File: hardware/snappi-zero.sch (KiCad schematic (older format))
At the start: 0 parts

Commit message: Design schematic.
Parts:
- added P1: CONN_02X40, symbol CONN_02X40
- added R1: 10k, symbol R
- added U1: RF200, symbol RF200
- added U2: SM220UF1, symbol SM220UF1
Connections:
- new net 3v3: P1.1 (P1), R1.1, U1.21 (VCC), U2.A2 (VCC), U2.A3 (VCC)
- new net GND: P1.9 (P9), U1.1 (GND), U1.24 (GND), U2.A1 (GND), U2.A8 (GND), U2.B8 (GND), U2.D8 (GND), U2.F8 (GND), U2.G8 (GND), U2.H1 (GND), U2.H8 (GND)
- new net GPIO_17: P1.11 (P11), R1.2, U1.23 (~RESET), U2.H5 (RESET)
- new net LED_A: U1.2 (GPIO0), U2.D1 (GPIO_5)
- new net LED_B: U1.3 (GPIO1), U2.D2 (GPIO_6)
- new net LED_C: U1.4 (GPIO2), U2.D3 (GPIO_7)
- new net PI_RX: P1.12 (P12), U1.10 (GPIO8)
- new net PI_TX: P1.10 (P10), U1.9 (GPIO7)
- no-connect marks 0 -> 120

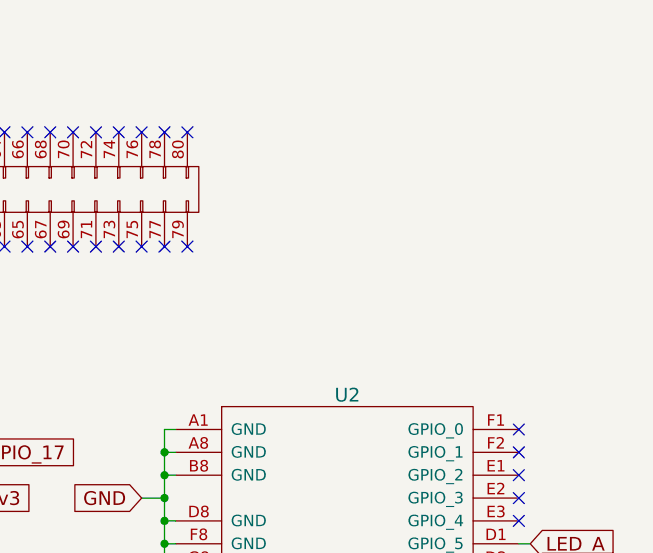
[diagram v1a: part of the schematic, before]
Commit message: Add LEDs and footprint assignment.
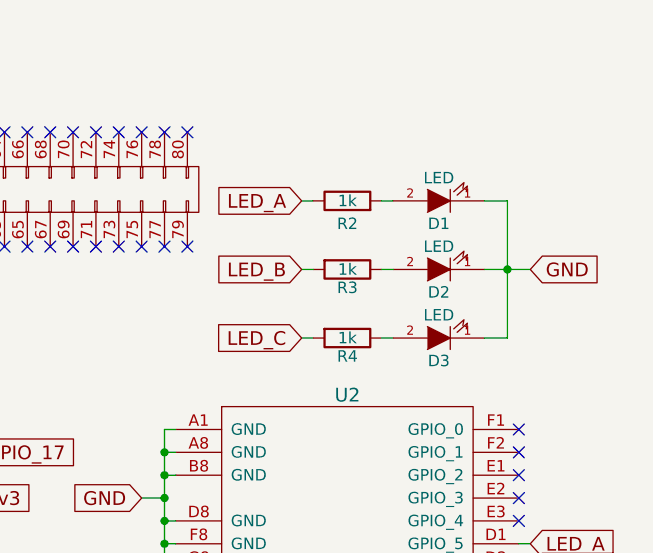
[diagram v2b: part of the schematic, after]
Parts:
- added D1, D2, D3: LED, LEDs:LED_1206, symbol LED
- added R2, R3, R4: 1k, Resistors_SMD:R_0805_HandSoldering, symbol R
- P1: footprint (none) -> Socket_Strips:Socket_Strip_Straight_2x40
- R1: footprint (none) -> Resistors_SMD:R_0805_HandSoldering
- U1: footprint (none) -> CrumpPrints:RF200
- U2: footprint (none) -> CrumpPrints:SM200
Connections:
- net GND: now also D1.1 (K), D2.1 (K), D3.1 (K)
- net LED_A: now also R2.1
- net LED_B: now also R3.2
- net LED_C: now also R4.2
- new net: D1.2 (A), R2.2
- new net: D2.2 (A), R3.1
- new net: D3.2 (A), R4.1
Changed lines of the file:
@@
 F 0 "P1" H 5400 3850 50  0000 C CNN
 F 1 "CONN_02X40" V 5400 1800 50  0000 C CNN
-F 2 "" H 5400 1800 50  0000 C CNN
+F 2 "Socket_Strips:Socket_Strip_Straight_2x40" H 5400 1800 50  0001 C CNN
 F 3 "" H 5400 1800 50  0000 C CNN
 	1    5400 1800
@@
 F 0 "U1" H 5500 2650 60  0000 C CNN
 F 1 "RF200" H 5500 4150 60  0000 C CNN
-F 2 "" H 5450 3400 60  0000 C CNN
+F 2 "CrumpPrints:RF200" H 5450 3400 60  0001 C CNN
 F 3 "" H 5450 3400 60  0000 C CNN
 	1    5500 3400
@@
 F 0 "U2" H 8050 6100 60  0000 C CNN
 F 1 "SM220UF1" H 8050 2250 60  0000 C CNN
-F 2 "" H 8750 5650 60  0000 C CNN
+F 2 "CrumpPrints:SM200" H 8750 5650 60  0001 C CNN
 F 3 "" H 8750 5650 60  0000 C CNN
 	1    8050 4400
@@
 F 0 "R1" V 6330 2800 50  0000 C CNN
 F 1 "10k" V 6250 2800 50  0000 C CNN
-F 2 "" V 6180 2800 50  0000 C CNN
+F 2 "Resistors_SMD:R_0805_HandSoldering" V 6180 2800 50  0001 C CNN
 F 3 "" H 6250 2800 50  0000 C CNN
 	1    6250 2800
@@
 Wire Wire Line
 	3400 3100 3400 3050
+$Comp
+L LED D1
+U 1 1 58832239
+P 8450 1850
+F 0 "D1" H 8450 1950 50  0000 C CNN
+F 1 "LED" H 8450 1750 50  0000 C CNN
+F 2 "LEDs:LED_1206" H 8450 1850 50  0001 C CNN
+F 3 "" H 8450 1850 50  0000 C CNN
+	1    8450 1850
+	-1   0    0    1
+$EndComp
+$Comp
+L LED D2
+U 1 1 58832292
+P 8450 2150
+F 0 "D2" H 8450 2250 50  0000 C CNN
+F 1 "LED" H 8450 2050 50  0000 C CNN
+F 2 "LEDs:LED_1206" H 8450 2150 50  0001 C CNN
+F 3 "" H 8450 2150 50  0000 C CNN
+	1    8450 2150
+	-1   0    0    1
+$EndComp
+$Comp
+L LED D3
+U 1 1 588322BD
+P 8450 2450
+F 0 "D3" H 8450 2550 50  0000 C CNN
+F 1 "LED" H 8450 2350 50  0000 C CNN
+F 2 "LEDs:LED_1206" H 8450 2450 50  0001 C CNN
+F 3 "" H 8450 2450 50  0000 C CNN
+	1    8450 2450
+	-1   0    0    1
+$EndComp
+Text GLabel 8850 2150 2    60   Input ~ 0
+GND
+Wire Wire Line
+	8650 1850 8750 1850
+Wire Wire Line
+	8750 1850 8750 2450
+Wire Wire Line
+	8650 2150 8850 2150
+Connection ~ 8750 2150
+Wire Wire Line
+	8750 2450 8650 2450
+$Comp
+L R R2
+U 1 1 588323E8
+P 8050 1850
+F 0 "R2" V 7950 1850 50  0000 C CNN
+F 1 "1k" V 8050 1850 50  0000 C CNN
+F 2 "Resistors_SMD:R_0805_HandSoldering" V 7980 1850 50  0001 C CNN
+F 3 "" H 8050 1850 50  0000 C CNN
+	1    8050 1850
+	0    -1   -1   0
+$EndComp
+$Comp
+L R R3
+U 1 1 58832419
+P 8050 2150
+F 0 "R3" V 8130 2150 50  0000 C CNN
+F 1 "1k" V 8050 2150 50  0000 C CNN
+F 2 "Resistors_SMD:R_0805_HandSoldering" V 7980 2150 50  0001 C CNN
+F 3 "" H 8050 2150 50  0000 C CNN
+	1    8050 2150
+	0    1    1    0
+$EndComp
+$Comp
+L R R4
+U 1 1 58832450
+P 8050 2450
+F 0 "R4" V 8130 2450 50  0000 C CNN
+F 1 "1k" V 8050 2450 50  0000 C CNN
+F 2 "Resistors_SMD:R_0805_HandSoldering" V 7980 2450 50  0001 C CNN
+F 3 "" H 8050 2450 50  0000 C CNN
+	1    8050 2450
+	0    1    1    0
+$EndComp
+Text GLabel 7850 1850 0    60   Input ~ 0
+LED_A
+Text GLabel 7850 2150 0    60   Input ~ 0
+LED_B
+Text GLabel 7850 2450 0    60   Input ~ 0
+LED_C
+Wire Wire Line
+	7850 1850 7900 1850
+Wire Wire Line
+	7850 2150 7900 2150
+Wire Wire Line
+	7850 2450 7900 2450
+Wire Wire Line
+	8200 2450 8250 2450
+Wire Wire Line
+	8200 2150 8250 2150
+Wire Wire Line
+	8200 1850 8250 1850
 $EndSCHEMATC

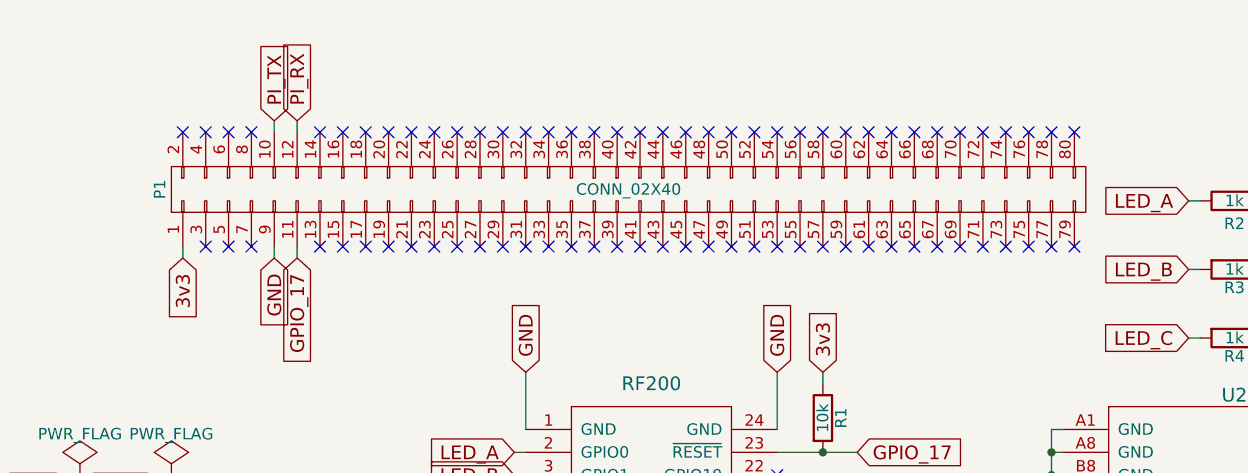
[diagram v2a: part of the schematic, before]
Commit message: Fix Pi Zero connector pin count.
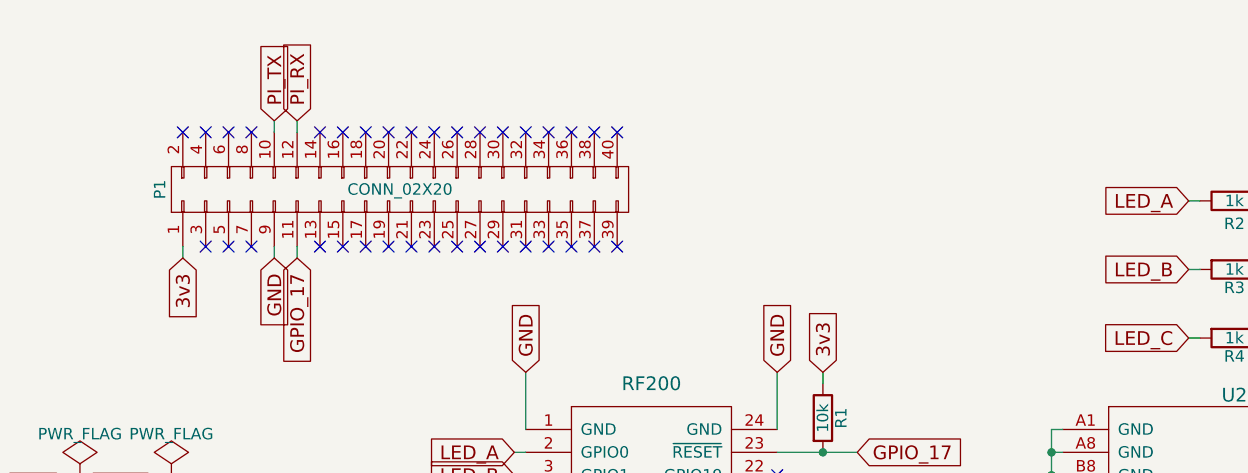
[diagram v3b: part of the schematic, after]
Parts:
- removed P1: CONN_02X40, Socket_Strips:Socket_Strip_Straight_2x40, symbol CONN_02X40
- added P1: CONN_02X20, symbol CONN_02X20
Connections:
- net 3v3: now also P1.1 (P1)
- net GND: now also P1.9 (P9)
- net GPIO_17: now also P1.11 (P11)
- net PI_RX: now also P1.12 (P12)
- net PI_TX: now also P1.10 (P10)
- no-connect marks 120 -> 80
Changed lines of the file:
@@
 Comment4 ""
 $EndDescr
-$Comp
-L CONN_02X40 P1
-U 1 1 5882E5C9
-P 5400 1800
-F 0 "P1" H 5400 3850 50  0000 C CNN
-F 1 "CONN_02X40" V 5400 1800 50  0000 C CNN
-F 2 "Socket_Strips:Socket_Strip_Straight_2x40" H 5400 1800 50  0001 C CNN
-F 3 "" H 5400 1800 50  0000 C CNN
-	1    5400 1800
-	0    -1   -1   0
-$EndComp
 Text GLabel 3450 2100 3    60   Input ~ 0
 3v3
@@
 NoConn ~ 5250 1550
 NoConn ~ 5350 1550
-NoConn ~ 5450 1550
-NoConn ~ 5550 1550
-NoConn ~ 5650 1550
-NoConn ~ 5750 1550
-NoConn ~ 5850 1550
-NoConn ~ 5950 1550
-NoConn ~ 6050 1550
-NoConn ~ 6150 1550
-NoConn ~ 6250 1550
-NoConn ~ 6350 1550
-NoConn ~ 6450 1550
-NoConn ~ 6550 1550
-NoConn ~ 6650 1550
-NoConn ~ 6750 1550
-NoConn ~ 6850 1550
-NoConn ~ 6950 1550
-NoConn ~ 7050 1550
-NoConn ~ 7150 1550
-NoConn ~ 7250 1550
-NoConn ~ 7350 1550
 NoConn ~ 4050 2050
 NoConn ~ 4150 2050
@@
 NoConn ~ 5250 2050
 NoConn ~ 5350 2050
-NoConn ~ 5450 2050
-NoConn ~ 5550 2050
-NoConn ~ 5650 2050
-NoConn ~ 5750 2050
-NoConn ~ 5850 2050
-NoConn ~ 5950 2050
-NoConn ~ 6050 2050
-NoConn ~ 6150 2050
-NoConn ~ 6250 2050
-NoConn ~ 6350 2050
-NoConn ~ 6450 2050
-NoConn ~ 6550 2050
-NoConn ~ 6650 2050
-NoConn ~ 6750 2050
-NoConn ~ 6850 2050
-NoConn ~ 6950 2050
-NoConn ~ 7050 2050
-NoConn ~ 7150 2050
-NoConn ~ 7250 2050
-NoConn ~ 7350 2050
 NoConn ~ 3550 2050
 NoConn ~ 3650 2050
@@
 Wire Wire Line
 	8200 1850 8250 1850
+$Comp
+L CONN_02X20 P1
+U 1 1 588480EC
+P 4400 1800
+F 0 "P1" H 4400 2850 50  0000 C CNN
+F 1 "CONN_02X20" V 4400 1800 50  0000 C CNN
+F 2 "" H 4400 850 50  0000 C CNN
+F 3 "" H 4400 850 50  0000 C CNN
+	1    4400 1800
+	0    -1   -1   0
+$EndComp
 $EndSCHEMATC

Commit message: Place and route initial board.
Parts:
- D1: value LED -> A
- D2: value LED -> B
- D3: value LED -> C
- P1: footprint (none) -> CrumpPrints:Raspberry_Pi_Zero
- U1: footprint CrumpPrints:RF200 -> CrumpPrints:RF200_nosilk
- U2: footprint CrumpPrints:SM200 -> CrumpPrints:SM200_nosilk
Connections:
- net LED_A: now also U1.4 (GPIO2), U2.D3 (GPIO_7); no longer U1.2 (GPIO0), U2.D1 (GPIO_5)
- net LED_C: now also U1.2 (GPIO0), U2.D1 (GPIO_5); no longer U1.4 (GPIO2), U2.D3 (GPIO_7)
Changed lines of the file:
@@
 F 0 "U1" H 5500 2650 60  0000 C CNN
 F 1 "RF200" H 5500 4150 60  0000 C CNN
-F 2 "CrumpPrints:RF200" H 5450 3400 60  0001 C CNN
+F 2 "CrumpPrints:RF200_nosilk" H 5450 3400 60  0001 C CNN
 F 3 "" H 5450 3400 60  0000 C CNN
 	1    5500 3400
@@
 F 0 "U2" H 8050 6100 60  0000 C CNN
 F 1 "SM220UF1" H 8050 2250 60  0000 C CNN
-F 2 "CrumpPrints:SM200" H 8750 5650 60  0001 C CNN
+F 2 "CrumpPrints:SM200_nosilk" H 8750 5650 60  0001 C CNN
 F 3 "" H 8750 5650 60  0000 C CNN
 	1    8050 4400
@@
 GPIO_17
 Text GLabel 4900 2950 0    60   Input ~ 0
-LED_A
+LED_C
 Text GLabel 4900 3050 0    60   Input ~ 0
 LED_B
 Text GLabel 4900 3150 0    60   Input ~ 0
+LED_A
+Text GLabel 8850 3350 2    60   Input ~ 0
 LED_C
-Text GLabel 8850 3350 2    60   Input ~ 0
-LED_A
 Text GLabel 8850 3450 2    60   Input ~ 0
 LED_B
 Text GLabel 8850 3550 2    60   Input ~ 0
-LED_C
+LED_A
 Wire Wire Line
 	3450 2050 3450 2100
@@
 P 8450 1850
 F 0 "D1" H 8450 1950 50  0000 C CNN
-F 1 "LED" H 8450 1750 50  0000 C CNN
+F 1 "A" H 8450 1750 50  0000 C CNN
 F 2 "LEDs:LED_1206" H 8450 1850 50  0001 C CNN
 F 3 "" H 8450 1850 50  0000 C CNN
@@
 P 8450 2150
 F 0 "D2" H 8450 2250 50  0000 C CNN
-F 1 "LED" H 8450 2050 50  0000 C CNN
+F 1 "B" H 8450 2050 50  0000 C CNN
 F 2 "LEDs:LED_1206" H 8450 2150 50  0001 C CNN
 F 3 "" H 8450 2150 50  0000 C CNN
@@
 P 8450 2450
 F 0 "D3" H 8450 2550 50  0000 C CNN
-F 1 "LED" H 8450 2350 50  0000 C CNN
+F 1 "C" H 8450 2350 50  0000 C CNN
 F 2 "LEDs:LED_1206" H 8450 2450 50  0001 C CNN
 F 3 "" H 8450 2450 50  0000 C CNN
@@
 F 0 "P1" H 4400 2850 50  0000 C CNN
 F 1 "CONN_02X20" V 4400 1800 50  0000 C CNN
-F 2 "" H 4400 850 50  0000 C CNN
+F 2 "CrumpPrints:Raspberry_Pi_Zero" H 4400 850 50  0001 C CNN
 F 3 "" H 4400 850 50  0000 C CNN
 	1    4400 1800

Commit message: Fix missing TX/RX pins on SM modules.
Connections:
- net PI_RX: now also U2.H4 (GPIO_11)
- net PI_TX: now also U2.G4 (GPIO_10)
- no-connect marks 80 -> 78
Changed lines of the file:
@@
 NoConn ~ 8800 3650
 NoConn ~ 8800 3750
-NoConn ~ 8800 3850
-NoConn ~ 8800 3950
 NoConn ~ 8800 4050
 NoConn ~ 8800 4150
@@
 	0    -1   -1   0
 $EndComp
+Text GLabel 8850 3850 2    60   Input ~ 0
+PI_TX
+Wire Wire Line
+	8800 3850 8850 3850
+Text GLabel 8850 3950 2    60   Input ~ 0
+PI_RX
+Wire Wire Line
+	8800 3950 8850 3950
 $EndSCHEMATC

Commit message: Fix Pi RX/TX pins.
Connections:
- net PI_RX: now also P1.10 (P10); no longer P1.12 (P12)
- net PI_TX: now also P1.8 (P8); no longer P1.10 (P10)
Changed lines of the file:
@@
 Text GLabel 3850 2100 3    60   Input ~ 0
 GND
-Text GLabel 3950 1500 1    60   Input ~ 0
+Text GLabel 3850 1500 1    60   Input ~ 0
 PI_RX
-Text GLabel 3850 1500 1    60   Input ~ 0
+Text GLabel 3750 1500 1    60   Input ~ 0
 PI_TX
 Text GLabel 3950 2100 3    60   Input ~ 0
@@
 	3850 1550 3850 1500
 Wire Wire Line
-	3950 1550 3950 1500
-Wire Wire Line
 	3950 2100 3950 2050
 Wire Wire Line
@@
 NoConn ~ 3550 1550
 NoConn ~ 3650 1550
-NoConn ~ 3750 1550
 NoConn ~ 4050 1550
 NoConn ~ 4150 1550
@@
 Wire Wire Line
 	8800 3950 8850 3950
+NoConn ~ 3950 1550
+Wire Wire Line
+	3750 1550 3750 1500
 $EndSCHEMATC
